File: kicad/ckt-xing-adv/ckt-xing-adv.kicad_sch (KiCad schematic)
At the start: 82 parts, among them J1 Screw_Terminal_01x02, J2 SM04B-SRSS, J3 Conn_02x05_Counter_Clockwise, J4 SM04B-SRSS, J5 SM04B-SRSS, J7 Screw_Terminal_01x02, Q1 ZXMS6004FF, Q2 ZXMS6004FF, U1 PAM8301, U2 ATtiny861A-S, U3 AP7381-33Y, U4 W25Q128JVS

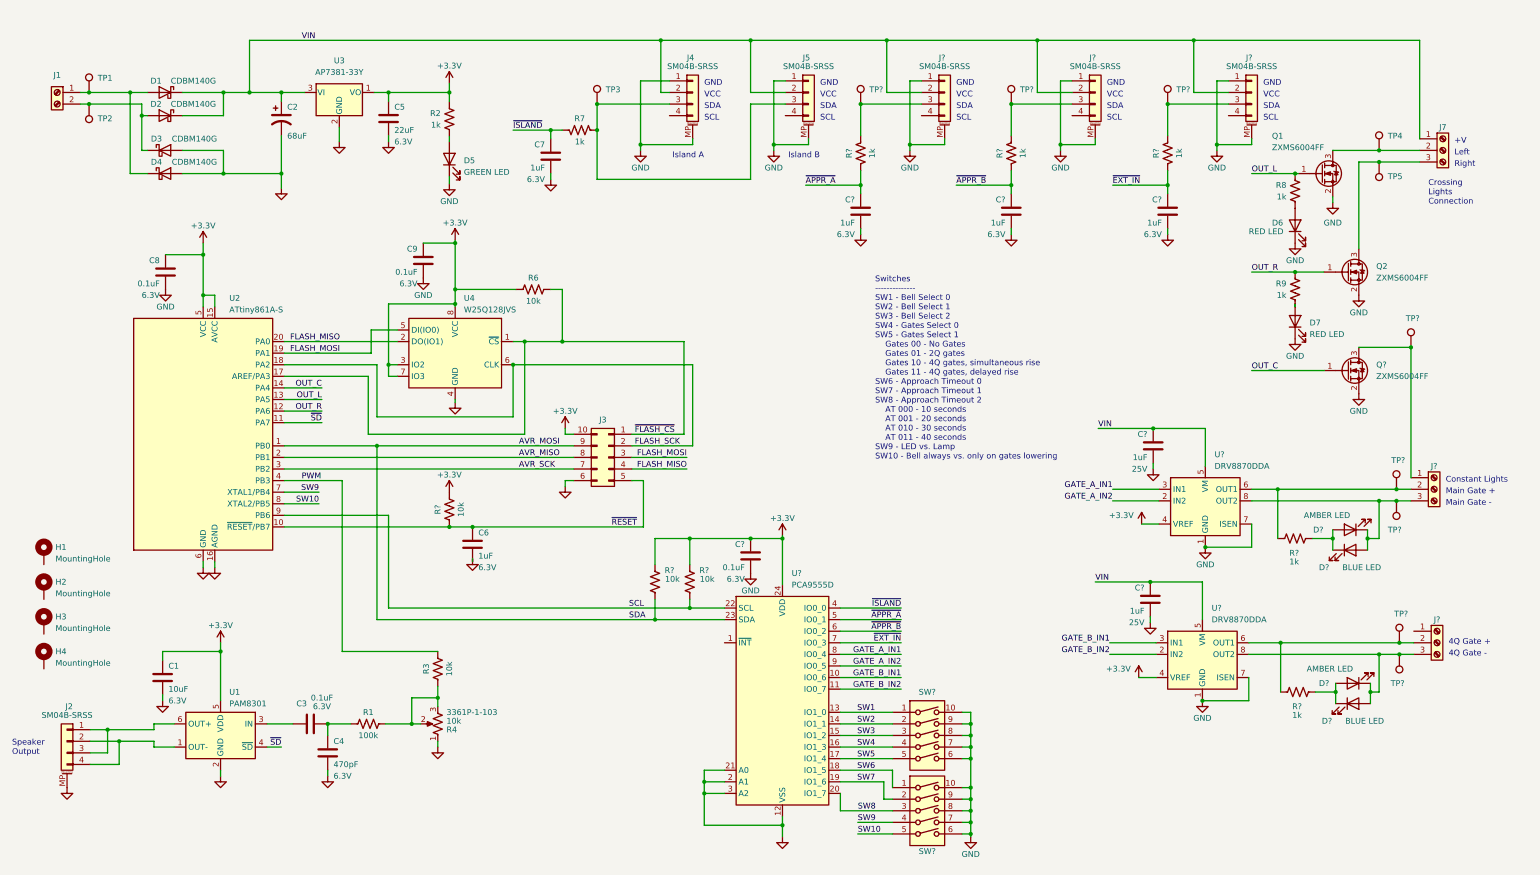
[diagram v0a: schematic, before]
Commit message: New full-featured xing plan
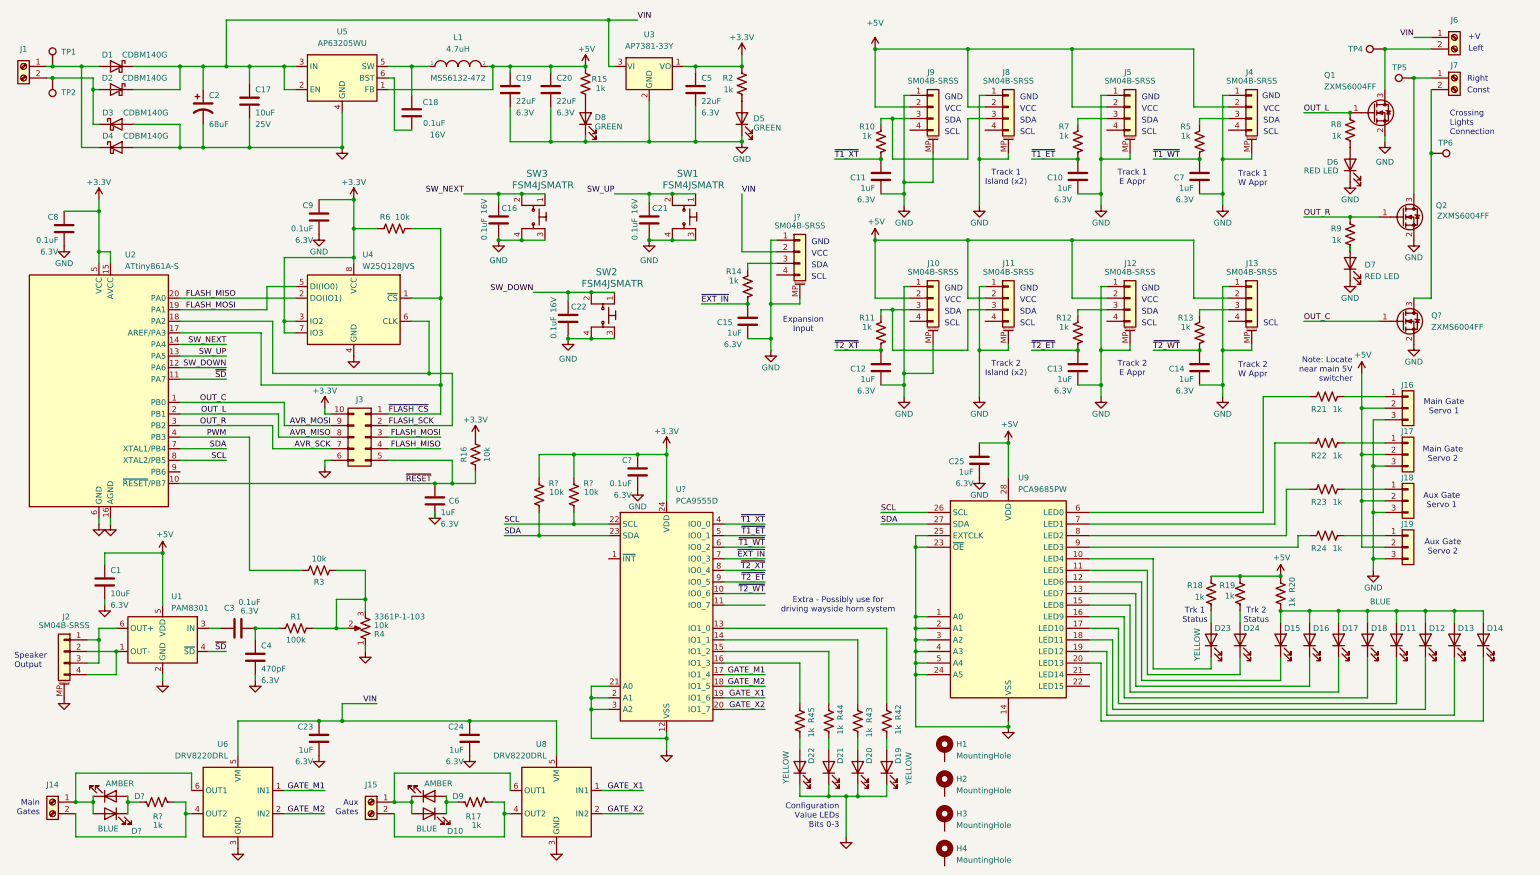
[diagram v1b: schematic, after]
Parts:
- removed C? (x5): 1uF, Capacitor_SMD:C_0805_2012Metric, symbol Device:C
- removed D?: BLUE LED, LED_SMD:LED_0805_2012Metric, symbol Device:LED
- removed D?: AMBER LED, LED_SMD:LED_0805_2012Metric, symbol Device:LED
- removed J7, J? (x2): Screw_Terminal_01x02, TerminalBlock_MetzConnect:TerminalBlock_MetzConnect_Type059_RT06303HBWC_1x03_P3.50mm_Horizontal, symbol Connector:Screw_Terminal_01x03
- removed J? (x2): SM04B-SRSS, Connector_JST:JST_SH_SM04B-SRSS-TB_1x04-1MP_P1.00mm_Horizontal, symbol Connector_Generic_MountingPin:Conn_01x04_MountingPin
- removed R? (x4): 1k, Resistor_SMD:R_0805_2012Metric, symbol Device:R_US
- removed R?: 10k, Resistor_SMD:R_0805_2012Metric, symbol Device:R_US
- removed SW? (x2): SW_DIP_x05, ISE_UltraLibrarian:CST_219SMT, symbol Switch:SW_DIP_x05
- removed TP3, TP? (x8): TestPoint, TestPoint:TestPoint_Pad_D2.0mm, symbol Connector:TestPoint
- removed U? (x2): DRV8870DDA, Package_SO:Texas_HTSOP-8-1EP_3.9x4.9mm_P1.27mm_EP2.95x4.9mm_Mask2.4x3.1mm_ThermalVias, symbol Driver_Motor:DRV8870DDA
- added C10, C11, C12, C13, C14, C15, C23, C24, C25: 1uF, Capacitor_SMD:C_0805_2012Metric, symbol Device:C
- added C16, C18, C21, C22: 0.1uF, Capacitor_SMD:C_0805_2012Metric, symbol Device:C
- added C17: 10uF, Capacitor_SMD:C_0805_2012Metric, symbol Device:C
- added C19, C20: 22uF, Capacitor_SMD:C_0805_2012Metric, symbol Device:C
- added D10, D11: BLUE, LED_SMD:LED_0805_2012Metric, symbol Device:LED
- added D12, D13, D14, D15, D16, D17, D18, D19, D20, D21, D22, D23, D24: YELLOW, LED_SMD:LED_0805_2012Metric, symbol Device:LED
- added D8: GREEN, LED_SMD:LED_0805_2012Metric, symbol Device:LED
- added D9: AMBER, LED_SMD:LED_0805_2012Metric, symbol Device:LED
- added J10, J11, J12, J13, J8, J9: SM04B-SRSS, Connector_JST:JST_SH_SM04B-SRSS-TB_1x04-1MP_P1.00mm_Horizontal, symbol Connector_Generic_MountingPin:Conn_01x04_MountingPin
- added J14, J15, J6, J7: Screw_Terminal_01x02, TerminalBlock_RND:TerminalBlock_RND_205-00012_1x02_P5.00mm_Horizontal, symbol Connector:Screw_Terminal_01x02
- added J16, J17, J18, J19: Conn_01x03, symbol Connector_Generic:Conn_01x03
- added L1: 4.7uH, ISE_UltraLibrarian:MSS6132-xxxMLC, symbol pspice:INDUCTOR
- added R10, R11, R12, R13, R14, R15, R17, R18, R19, R20, R21, R22, R23, R24, R42, R43, R44, R45, R5: 1k, Resistor_SMD:R_0805_2012Metric, symbol Device:R_US
- added R16: 10k, Resistor_SMD:R_0805_2012Metric, symbol Device:R_US
- added SW1, SW2, SW3: FSM4JSMATR, ISE_Generic:TE_FSM4JSMA, symbol dk_Tactile-Switches:FSM4JSMATR
- added TP6: TestPoint, TestPoint:TestPoint_Pad_D2.0mm, symbol Connector:TestPoint
- added U5: AP63205WU, Package_TO_SOT_SMD:TSOT-23-6, symbol Regulator_Switching:AP63203WU
- added U6, U8: DRV8220DRL, Package_TO_SOT_SMD:SOT-563, symbol Driver_Motor:DRV8220DRL
- added U9: PCA9685PW, Package_SO:TSSOP-28_4.4x9.7mm_P0.65mm, symbol Driver_LED:PCA9685PW
- D5: value GREEN LED -> GREEN
- D?: value AMBER LED -> AMBER
- D?: value BLUE LED -> BLUE
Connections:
- net SW10 is gone; now on net SCL: U2.8 (XTAL2/PB5)
- net +3.3V: now also R16.2; no longer C1.1, U1.5 (VDD)
- net AVR_MISO: now also Q1.1 (G), R8.2
- net AVR_MOSI: now also Q?.1 (G); no longer R?.1, U?.23 (SDA)
- net AVR_SCK: now also Q2.1 (G), R9.2
- net GND: now also C10.2, C11.2, C12.2, C13.2, C14.2, C15.2, C16.2, C17.2, C19.2, C20.2, C21.2, C22.2, C23.2, C24.2, C25.2, D19.1 (K), D20.1 (K), D21.1 (K), D22.1 (K), D8.1 (K), J10.1 (Pin_1), J10.MP (MountPin), J11.1 (Pin_1), J11.MP (MountPin), J12.1 (Pin_1), J12.MP (MountPin), J13.1 (Pin_1), J13.MP (MountPin), J16.3 (Pin_3), J17.3 (Pin_3), J18.3 (Pin_3), J19.3 (Pin_3), J8.1 (Pin_1), J8.MP (MountPin), J9.1 (Pin_1), J9.MP (MountPin), SW1.3, SW1.4, SW2.3, SW2.4, SW3.3, SW3.4, U5.4 (GND), U6.3 (GND), U8.3 (GND), U9.1 (A0), U9.14 (VSS), U9.2 (A1), U9.23 (~{OE}), U9.24 (A5), U9.25 (EXTCLK), U9.3 (A2), U9.4 (A3), U9.5 (A4)
- net SCL: now also U9.26 (SCL); no longer U2.9 (PB6)
- net VIN: now also C17.1, C23.1, C24.1, J6.1 (Pin_1), U5.2 (EN), U5.3 (IN), U6.5 (VM), U8.5 (VM); no longer J4.2 (Pin_2), J5.2 (Pin_2)
- net ~{EXT_IN}: now also C15.1, R14.2
- net ~{RESET}: now also R16.1
- net at Q1.3 (D), TP4.1: now also J6.2 (Pin_2)
- net at Q2.3 (D), TP5.1: now also J7.1 (Pin_1)
- net at D?.1 (K), D?.2 (A): now also J14.1 (Pin_1), U6.6 (OUT1)
- net at J?.3 (Pin_3): now also R14.1
- net at J5.3 (Pin_3), R7.1: no longer J4.3 (Pin_3)
- net at R?.2: now also J14.2 (Pin_2), U6.4 (OUT2)
- net at Q?.3 (D): now also J7.2 (Pin_2), TP6.1
- net GATE_A_IN1 renamed ~{T2_XT}
- net ~{T2_XT}: now also C12.1, R11.2
- net GATE_A_IN2 renamed ~{T2_ET}
- net ~{T2_ET}: now also C13.1, R12.2
- net GATE_B_IN1 renamed ~{T2_WT}
- net ~{T2_WT}: now also C14.1, R13.2
- net GATE_B_IN2: no longer names the net of U?.11 (IO0_7)
- net OUT_C renamed SW_NEXT
- net SW_NEXT: now also C16.1, SW3.1, SW3.2; no longer Q?.1 (G)
- removed net OUT_L: Q1.1 (G), R8.2, U2.13 (PA5)
- removed net OUT_R: Q2.1 (G), R9.2, U2.12 (PA6)
- net SW1: no longer names the net of U?.13 (IO1_0)
- net SW1: now also R42.1
- net SW2: no longer names the net of U?.14 (IO1_1)
- net SW2: now also R43.1
- net SW3: no longer names the net of U?.15 (IO1_2)
- net SW3: now also R44.1
- net SW4: no longer names the net of U?.16 (IO1_3)
- net SW4: now also R45.1
- net SW5 renamed GATE_M1
- net GATE_M1: now also U6.1 (IN1)
- net SW6 renamed GATE_M2
- net GATE_M2: now also U6.2 (IN2)
- net SW7 renamed GATE_X1
- net GATE_X1: now also U8.1 (IN1)
- net SW8 renamed GATE_X2
- net GATE_X2: now also U8.2 (IN2)
- net SW9 renamed SDA
- net SDA: now also R?.1, U?.23 (SDA), U9.27 (SDA)
- net ~{APPR_A} renamed ~{T1_ET}
- net ~{T1_ET}: now also R7.2, C10.1
- net ~{APPR_B} renamed ~{T1_WT}
- net ~{T1_WT}: now also C7.1, R5.2
- removed net ~{ISLAND}: C7.1, R7.2, U?.4 (IO0_0)
- new net: D15.1 (K), U9.12 (LED6)
- new net: D11.2 (A), D12.2 (A), D13.2 (A), D14.2 (A), D15.2 (A), D16.2 (A), D17.2 (A), D18.2 (A), R20.2
- new net: J16.1 (Pin_1), R21.2
- new net: C18.1, L1.1, U5.5 (SW)
- new net: C18.2, U5.6 (BST)
- new net: D20.2 (A), R43.2
- new net: D17.1 (K), U9.15 (LED8)
- new net: D22.2 (A), R45.2
- new net: J8.3 (Pin_3), J9.3 (Pin_3), R10.1
- new net: D19.2 (A), R42.2
- new net: D13.1 (K), U9.19 (LED12)
- new net: D10.1 (K), D9.2 (A), R17.1
- new net: D10.2 (A), D9.1 (K), J15.1 (Pin_1), U8.6 (OUT1)
- new net: D16.1 (K), U9.13 (LED7)
- new net: R23.1, U9.8 (LED2)
- new net: J18.1 (Pin_1), R23.2
- new net: D18.1 (K), U9.16 (LED9)
- new net: D21.2 (A), R44.2
- new net: D12.1 (K), U9.18 (LED11)
- new net: J15.2 (Pin_2), R17.2, U8.4 (OUT2)
- new net: J13.3 (Pin_3), R13.1
- new net: D11.1 (K), U9.17 (LED10)
- new net: R24.1, U9.9 (LED3)
- new net: J19.1 (Pin_1), R24.2
- new net: J10.3 (Pin_3), J11.3 (Pin_3), R11.1
- new net: J12.3 (Pin_3), R12.1
- new net: J17.1 (Pin_1), R22.2
- new net: D14.1 (K), U9.20 (LED13)
- new net: J4.3 (Pin_3), R5.1
- new net: R21.1, U9.6 (LED0)
- new net: D23.2 (A), R18.2
- new net: D23.1 (K), U9.10 (LED4)
- new net: D24.1 (K), U9.11 (LED5)
- new net: R22.1, U9.7 (LED1)
- new net: D8.2 (A), R15.1
- new net: D24.2 (A), R19.2
- new net +5V: C1.1, C19.1, C20.1, C25.1, J10.2 (Pin_2), J11.2 (Pin_2), J12.2 (Pin_2), J13.2 (Pin_2), J16.2 (Pin_2), J17.2 (Pin_2), J18.2 (Pin_2), J19.2 (Pin_2), J4.2 (Pin_2), J5.2 (Pin_2), J8.2 (Pin_2), J9.2 (Pin_2), L1.2, R15.2, R18.1, R19.1, R20.1, U1.5 (VDD), U5.1 (FB), U9.28 (VDD)
- new net SW_DOWN: C22.1, SW2.1, SW2.2, U2.12 (PA6)
- new net SW_UP: C21.1, SW1.1, SW1.2, U2.13 (PA5)
- new net ~{T1_XT}: C11.1, R10.2, U?.4 (IO0_0)
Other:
- note added: "Aux Gate Servo 1"
- note added: "Aux Gate Servo 2"
- note added: "Aux Gates"
- note added: "Configuration Value LEDs Bits 0-3"
- note added: "Const"
- note added: "Expansion Input"
- note added: "Extra - Possibly use for driving wayside horn system"
- note added: "Main Gate Servo 1"
- note added: "Main Gate Servo 2"
- note added: "Main Gates"
- note added: "Note: Locate near main 5V switcher"
- note added: "Track 1 E Appr"
- note added: "Track 1 Island (x2)"
- note added: "Track 1 W Appr"
- note added: "Track 2 E Appr"
- note added: "Track 2 Island (x2)"
- note added: "Track 2 W Appr"
- note added: "Trk 1 Status"
- note added: "Trk 2 Status"
- note removed: "4Q Gate +"
- note removed: "4Q Gate -"
- note removed: "Constant Lights"
- note removed: "Island A"
- note removed: "Island B"
- note removed: "Main Gate +"
- note removed: "Main Gate -"
- note removed: "Switches -------------- SW1 - Bell Select 0 SW2 - Bell Select 1 SW3 - Bell Select 2 SW4 - Gates Select 0 SW5 - Gates Select 1 Gates 00 - No Gates Gates 01 - 2Q gates Gates 10 - 4Q gates, simultaneous rise Gates 11 - 4Q gates, delayed rise SW6 - Approach Timeout 0 SW7 - Approach Timeout 1 SW8 - Approach Timeout 2 AT 000 - 10 seconds AT 001 - 20 seconds AT 010 - 30 seconds AT 011 - 40 seconds SW9 -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"
- moved on the sheet: C1, C2, C3, C4, C5, C6, C8, C9, C?, D1, D2, D3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

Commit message: Update advanced crossing with some fixes before PCB layout
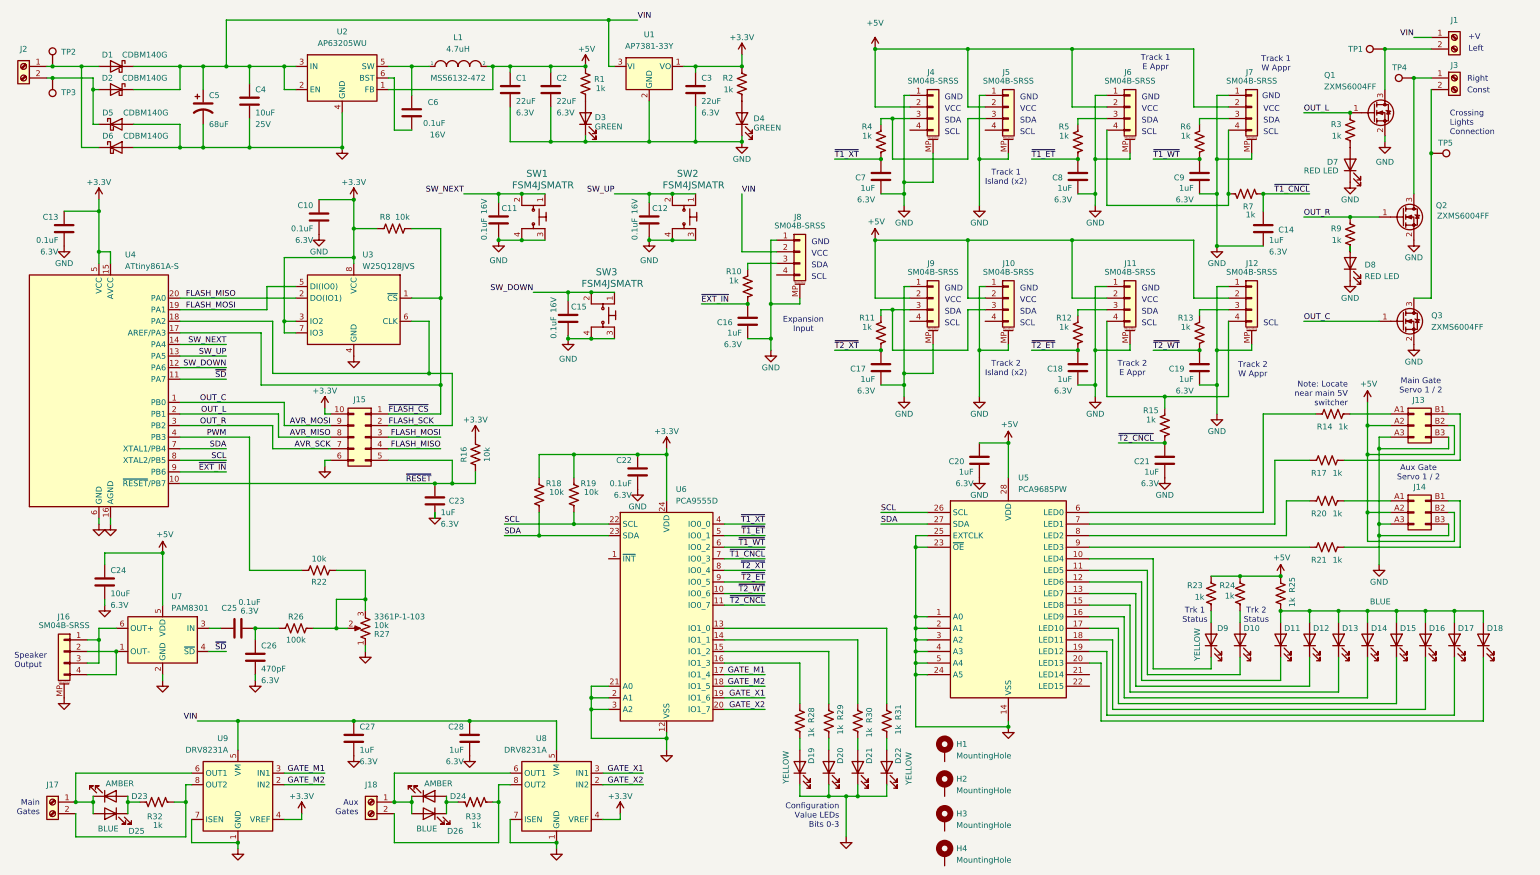
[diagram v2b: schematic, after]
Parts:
- removed J16, J17, J18, J19: Conn_01x03, symbol Connector_Generic:Conn_01x03
- removed U6, U8: DRV8220DRL, Package_TO_SOT_SMD:SOT-563, symbol Driver_Motor:DRV8220DRL
- added C14, C21: 1uF, Capacitor_SMD:C_0805_2012Metric, symbol Device:C
- added J13, J14: Conn_02x03_Row_Letter_First, ISE_UltraLibrarian:MOLEX_15910060, symbol ISE_Generic:MOLEX_15910060
- added R15, R7: 1k, Resistor_SMD:R_0805_2012Metric, symbol Device:R_US
- added U8, U9: DRV8231A, Package_SO:Texas_HTSOP-8-1EP_3.9x4.9mm_P1.27mm_EP2.95x4.9mm_Mask2.4x3.1mm_ThermalVias, symbol Driver_Motor:DRV8870DDA
- D1, D2: footprint Diode_SMD:D_SOD-123 -> ISE_Generic:SOD-123T
- D5: renamed from D3; footprint Diode_SMD:D_SOD-123 -> ISE_Generic:SOD-123T
- D6: renamed from D4; footprint Diode_SMD:D_SOD-123 -> ISE_Generic:SOD-123T
- U3: renamed from U4; footprint Package_SO:SOIC-8_5.23x5.23mm_P1.27mm -> Package_SO:SOIC-8_5.3x5.3mm_P1.27mm
- U6: renamed from U?; footprint Package_SO:SOIC-24W_7.5x15.4mm_P1.27mm -> Package_SO:TSSOP-24_4.4x7.8mm_P0.65mm
- gave numbers to parts that had none: 8
- renumbered C19 to C1, C9 to C10, C16 to C11, C21 to C12, C8 to C13, C22 to C15, C15 to C16, C12 to C17, C13 to C18, C14 to C19, C20 to C2, C25 to C20, C6 to C23, C1 to C24, C3 to C25, C4 to C26, C23 to C27, C24 to C28, C5 to C3, C17 to C4, C2 to C5, C18 to C6, C11 to C7, C10 to C8, C7 to C9, D24 to D10, D15 to D11, D16 to D12, D17 to D13, D18 to D14, D11 to D15, D12 to D16, D13 to D17, D14 to D18, D22 to D19, D21 to D20, D20 to D21, D19 to D22, D9 to D24, D10 to D26, D8 to D3, D5 to D4, D6 to D7, D7 to D8, D23 to D9, J6 to J1, J11 to J10, J12 to J11, J13 to J12, J3 to J15, J2 to J16, J14 to J17, J15 to J18, J1 to J2, J7 to J3, J9 to J4, J8 to J5, J5 to J6, J4 to J7, J10 to J9, R15 to R1, R14 to R10, R21 to R14, R22 to R17, R23 to R20, R24 to R21, R3 to R22, R18 to R23, R19 to R24, R20 to R25, R1 to R26, R4 to R27, R45 to R28, R44 to R29, R8 to R3, R43 to R30, R42 to R31, R17 to R33, R10 to R4, R7 to R5, R5 to R6, R6 to R8, SW3 to SW1, SW1 to SW2, SW2 to SW3, TP4 to TP1, TP1 to TP2, TP2 to TP3, TP5 to TP4, TP6 to TP5, U3 to U1, U5 to U2, U2 to U4, U9 to U5, U1 to U7
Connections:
- net +3.3V: now also U8.4 (VREF), U9.4 (VREF)
- net +5V: now also J13.A2 (Pin_a2), J13.B2 (Pin_b2), J14.A2 (Pin_a2), J14.B2 (Pin_b2)
- net GATE_M1: now also U9.3 (IN1)
- net GATE_M2: now also U9.2 (IN2)
- net GATE_X1: now also U8.3 (IN1)
- net GATE_X2: now also U8.2 (IN2)
- net GND: now also C14.2, C21.2, J13.A3 (Pin_a3), J13.B3 (Pin_b3), J14.A3 (Pin_a3), J14.B3 (Pin_b3), U8.1 (GND), U8.7 (ISEN), U8.9 (GND), U9.1 (GND), U9.7 (ISEN), U9.9 (GND)
- net VIN: now also U8.5 (VM), U9.5 (VM)
- net ~{EXT_IN}: now also U4.9 (PB6); no longer U6.7 (IO0_3)
- net at R14.2: now also J13.A1 (Pin_a1)
- net at D23.1 (K), D25.2 (A), J17.1 (Pin_1): now also U9.6 (OUT1)
- net at J17.2 (Pin_2), R32.2: now also U9.8 (OUT2)
- net at D24.1 (K), D26.2 (A), J18.1 (Pin_1): now also U8.6 (OUT1)
- net at R20.2: now also J14.A1 (Pin_a1)
- net at J18.2 (Pin_2), R33.2: now also U8.8 (OUT2)
- net at J6.4 (Pin_4): now also J7.4 (Pin_4), R7.1
- net at R21.2: now also J14.B1 (Pin_b1)
- net at J11.4 (Pin_4): now also J12.4 (Pin_4), R15.1
- net at R17.2: now also J13.B1 (Pin_b1)
- net ~{T2_CNCL}: now reaches U6.11 (IO0_7)
- net ~{T2_CNCL}: now also C21.1, R15.2
- new net ~{T1_CNCL}: C14.1, R7.2, U6.7 (IO0_3)
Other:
- note added: "Aux Gate Servo 1 / 2"
- note added: "Main Gate Servo 1 / 2"
- note removed: "Aux Gate Servo 1"
- note removed: "Aux Gate Servo 2"
- note removed: "Extra - Possibly use for driving wayside horn system"
- note removed: "Main Gate Servo 1"
- note removed: "Main Gate Servo 2"
- moved on the sheet: C27, R14, R17, R20, R21

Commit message: All nets routed on the ckt-xing-adv/ckt-xing-adv Still some DRC problems related to kicad 9
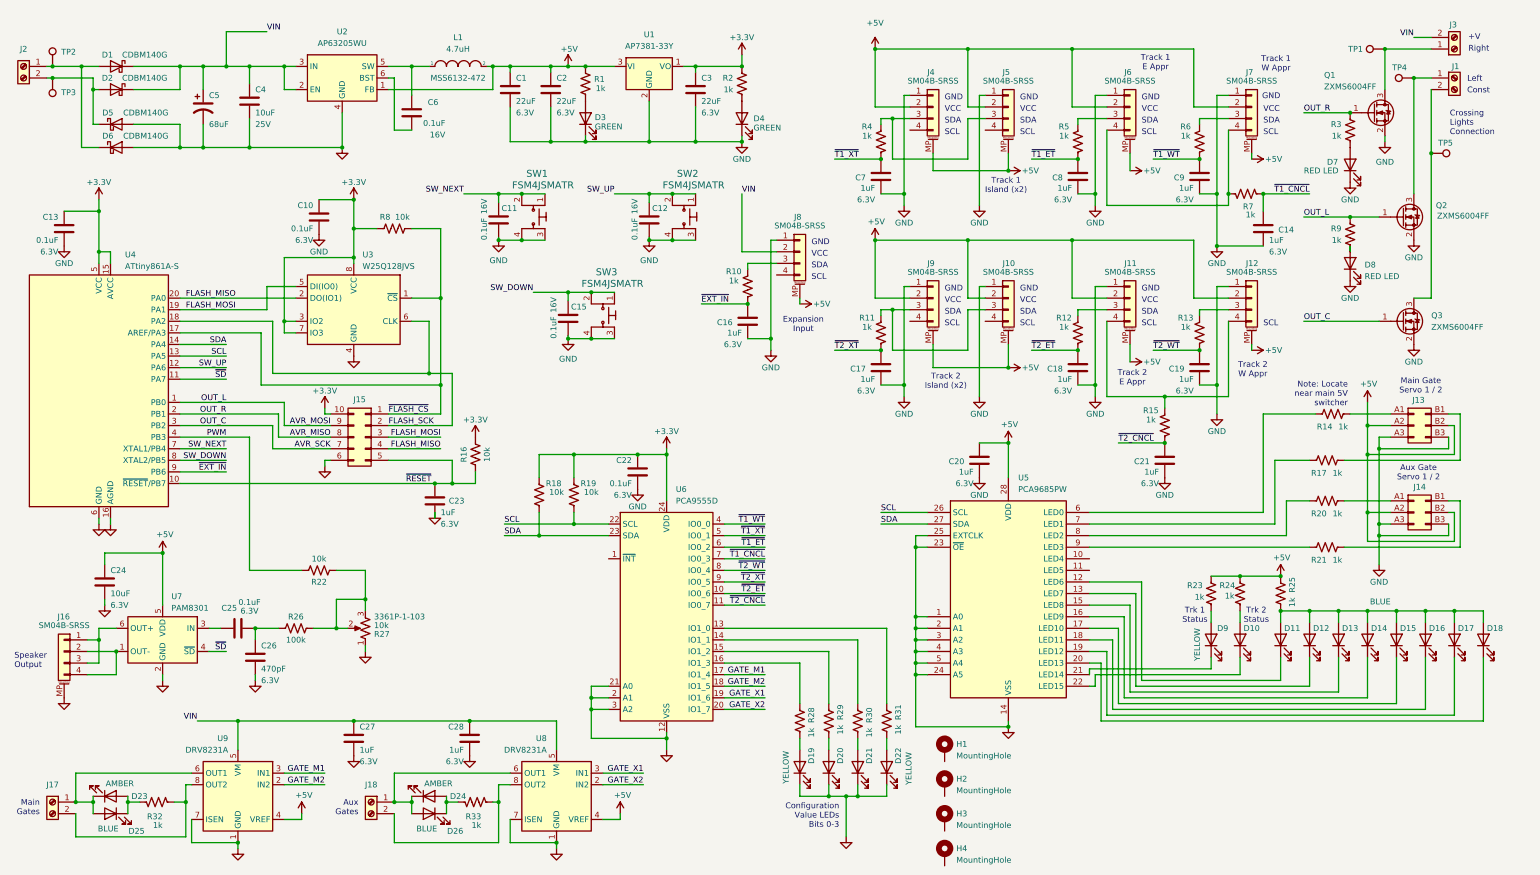
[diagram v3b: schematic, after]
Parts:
- U3: footprint Package_SO:SOIC-8_5.3x5.3mm_P1.27mm -> Package_SO:SOIC-8_5.3x6.2mm_P1.27mm
- renumbered J3 to J1, J1 to J3
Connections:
- net +3.3V: no longer U8.4 (VREF), U9.4 (VREF)
- net +5V: now also J10.MP (MountPin), J11.MP (MountPin), J12.MP (MountPin), J4.MP (MountPin), J5.MP (MountPin), J6.MP (MountPin), J7.MP (MountPin), J8.MP (MountPin), J9.MP (MountPin), U1.3 (VI), U8.4 (VREF), U9.4 (VREF)
- net AVR_MOSI: now also Q2.1 (G), R9.2; no longer Q3.1 (G)
- net AVR_SCK: now also Q3.1 (G); no longer Q2.1 (G), R9.2
- net GND: no longer J10.MP (MountPin), J11.MP (MountPin), J12.MP (MountPin), J4.MP (MountPin), J5.MP (MountPin), J6.MP (MountPin), J7.MP (MountPin), J8.MP (MountPin), J9.MP (MountPin)
- net SCL: now also U4.13 (PA5); no longer U4.8 (XTAL2/PB5)
- net SDA: now also U4.14 (PA4); no longer U4.7 (XTAL1/PB4)
- net SW_DOWN: now also U4.8 (XTAL2/PB5); no longer U4.12 (PA6)
- net SW_NEXT: now also U4.7 (XTAL1/PB4); no longer U4.14 (PA4)
- net SW_UP: now also U4.12 (PA6); no longer U4.13 (PA5)
- net VIN: now also J3.2 (Pin_2); no longer J3.1 (Pin_1), U1.3 (VI)
- net ~{T1_ET}: now also U6.6 (IO0_2); no longer U6.5 (IO0_1)
- net ~{T1_WT}: now also U6.4 (IO0_0); no longer U6.6 (IO0_2)
- net ~{T1_XT}: now also U6.5 (IO0_1); no longer U6.4 (IO0_0)
- net ~{T2_ET}: now also U6.10 (IO0_6); no longer U6.9 (IO0_5)
- net ~{T2_WT}: now also U6.8 (IO0_4); no longer U6.10 (IO0_6)
- net ~{T2_XT}: now also U6.9 (IO0_5); no longer U6.8 (IO0_4)
- net at Q1.3 (D), TP1.1: now also J3.1 (Pin_1); no longer J3.2 (Pin_2)
- net at U5.10 (LED4): no longer D9.1 (K)
- net at U5.11 (LED5): no longer D10.1 (K)
- net at U5.21 (LED14): now also D9.1 (K)
- net at U5.22 (LED15): now also D10.1 (K)
